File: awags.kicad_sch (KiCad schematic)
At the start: 30 parts

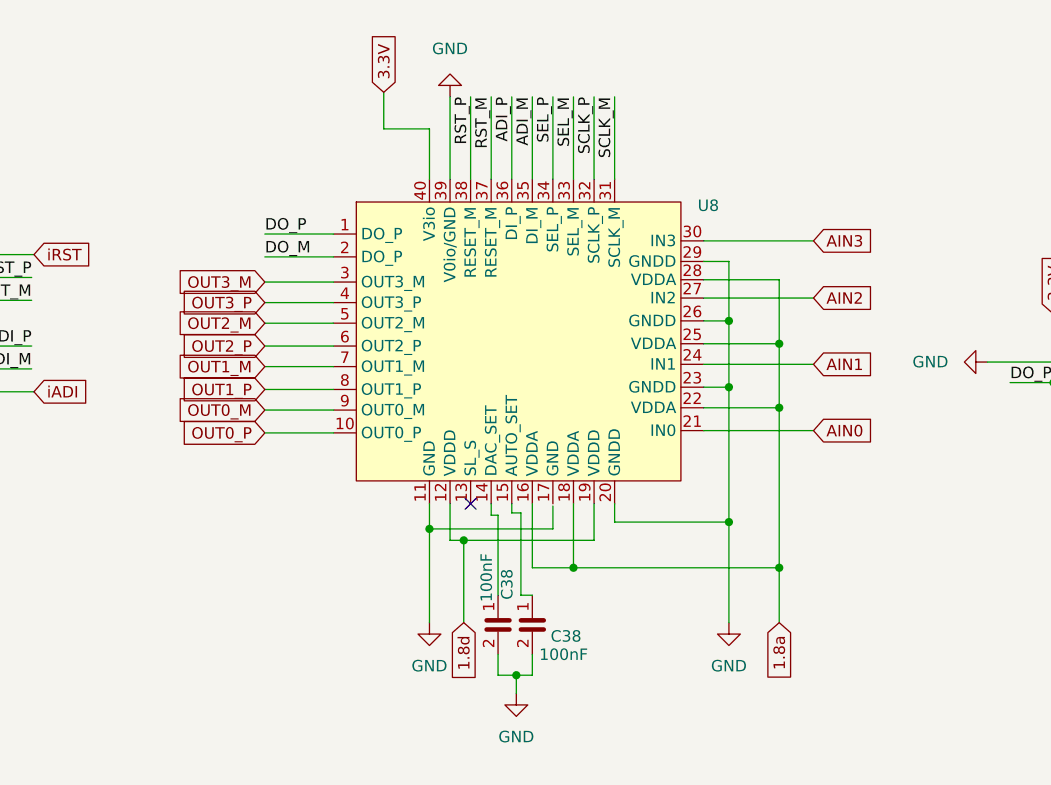
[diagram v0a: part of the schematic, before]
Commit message: Added DAC circuit.
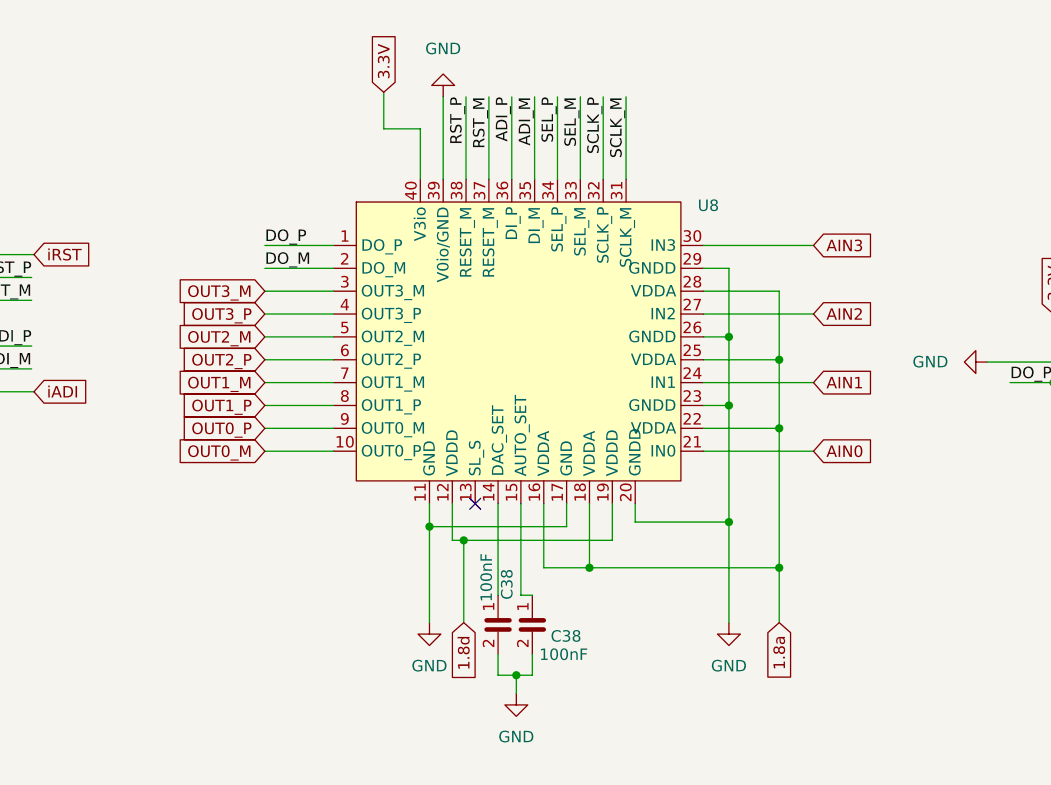
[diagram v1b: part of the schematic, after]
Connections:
- net GND: now also U8.17 (GND)
- net OUT0_M: now also U8.10 (OUT0_P); no longer U8.9 (OUT0_M)
- net OUT0_P: now also U8.9 (OUT0_M); no longer U8.10 (OUT0_P)

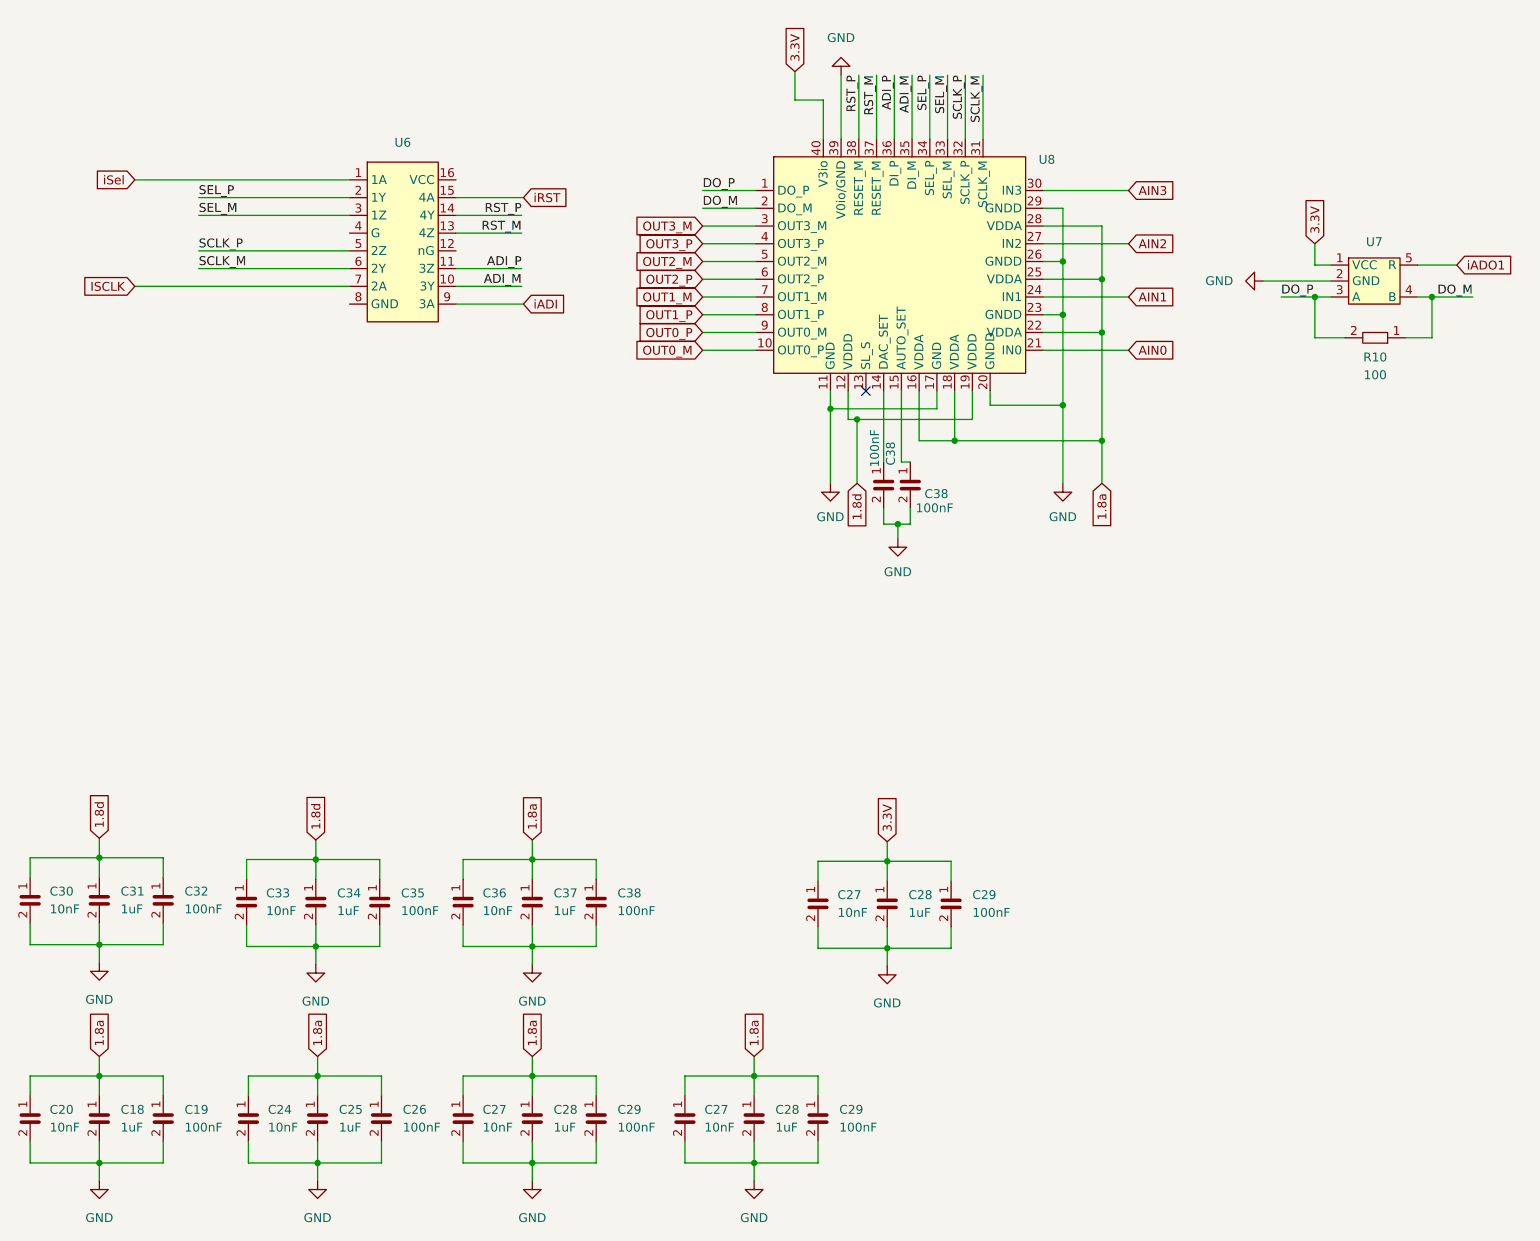
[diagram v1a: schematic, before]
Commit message: Changed global to hierarchichal lables, reorganized main sheet to get pins to connector.
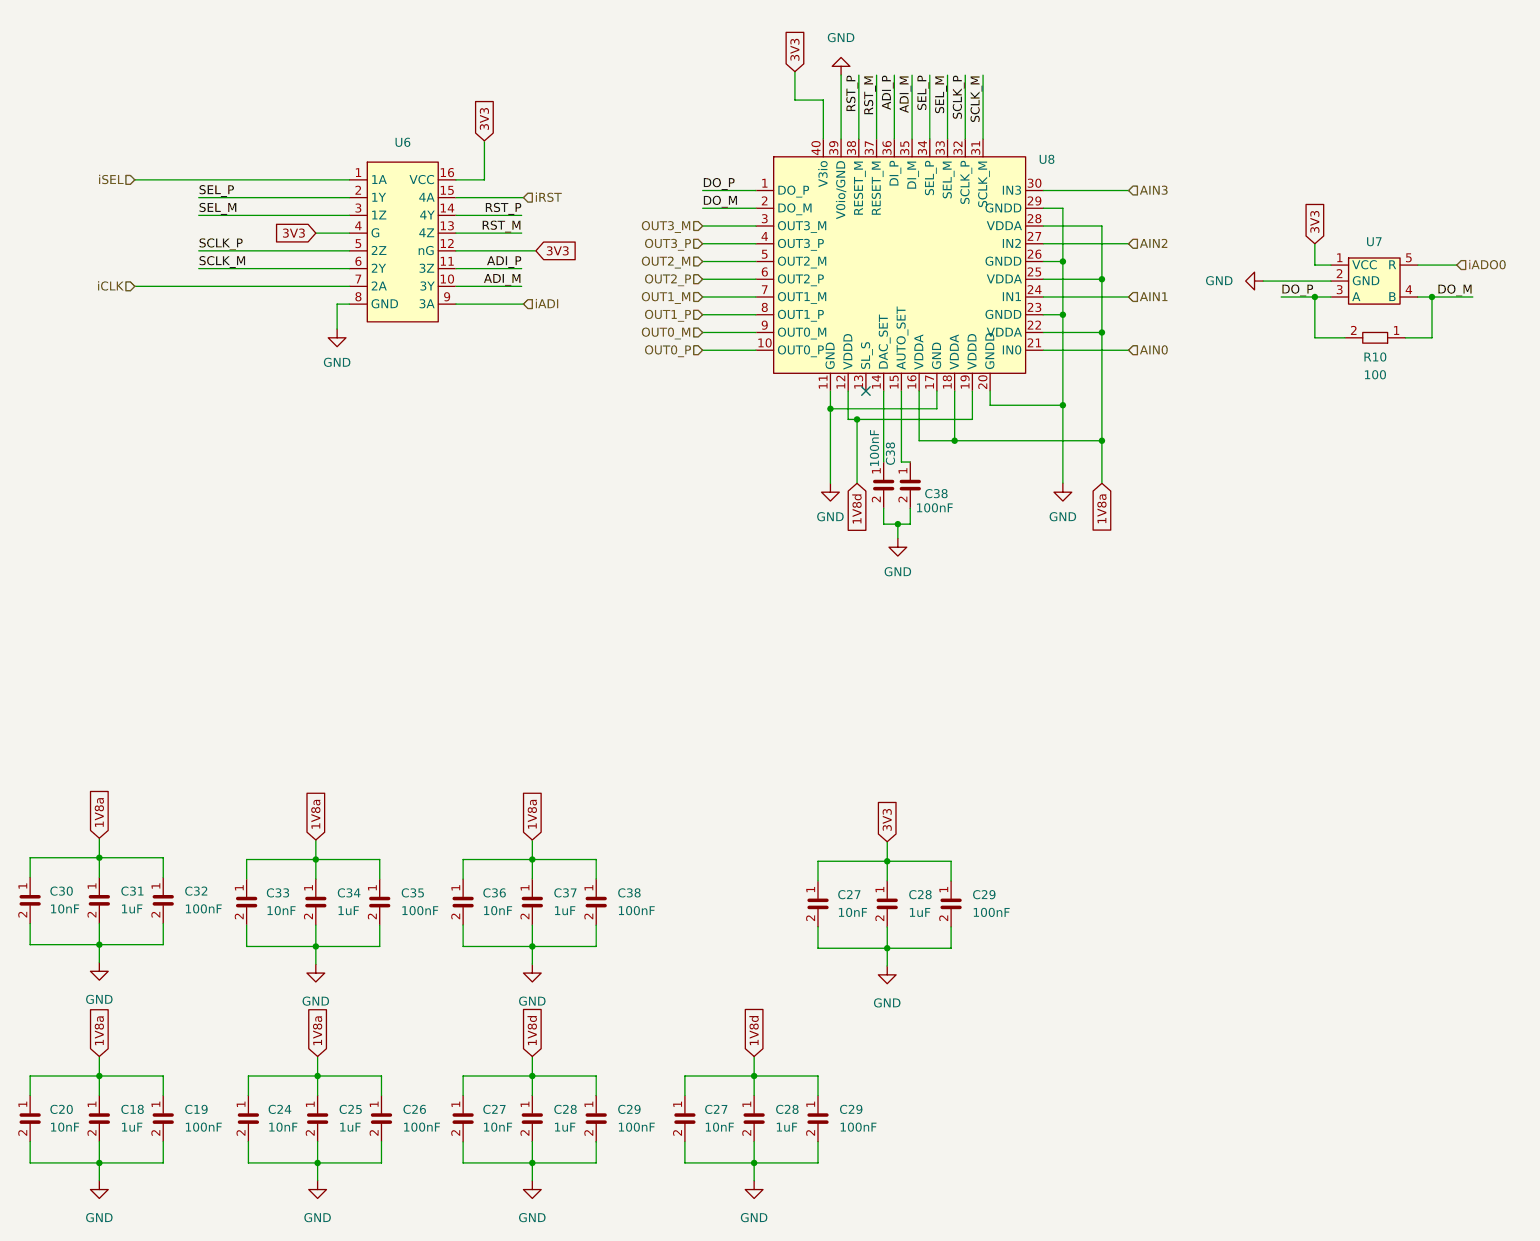
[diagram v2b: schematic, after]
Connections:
- net 3.3V is gone; now on net 3V3: C27.1, C28.1, C29.1, U7.1 (VCC), U8.40 (V3io)
- net GND: now also U6.8 (GND)
- net OUT0_M: now also U8.9 (OUT0_M); no longer U8.10 (OUT0_P)
- net OUT0_P: now also U8.10 (OUT0_P); no longer U8.9 (OUT0_M)
- net 3V3: now reaches U6.12 (nG)
- net 3V3: now also U6.16 (VCC), U6.4 (G)
- net 1.8a renamed 1V8a
- net 1V8a: now also C30.1, C31.1, C32.1, C33.1, C34.1, C35.1; no longer C27.1, C27.1, C28.1, C28.1, C29.1, C29.1
- removed net 1.8d: C30.1, C31.1, C32.1, C33.1, C34.1, C35.1, U8.12 (VDDD), U8.19 (VDDD)
- net ISCLK renamed iCLK
- net iADO1 renamed iADO0
- net iSel renamed iSEL
- new net 1V8d: C27.1, C27.1, C28.1, C28.1, C29.1, C29.1, U8.12 (VDDD), U8.19 (VDDD)

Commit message: Layout erster Entwurf fertig.
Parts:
- removed C18, C28: C0402_1uF_6.3V, Capacitor_SMD:C_0402_1005Metric, symbol Jojos_Lib:C0402_1uF_6.3V
- removed C19, C29: C0402_100nF_50V, Capacitor_SMD:C_0402_1005Metric, symbol Jojos_Lib:C0402_100nF_50V
- removed C20, C27: C0402_10nF_16V, Capacitor_SMD:C_0402_1005Metric, symbol Jojos_Lib:C0402_10nF_16V
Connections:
- net 1V8d is gone; now on net 1V8a: C27.1, C28.1, C29.1, U8.12 (VDDD), U8.19 (VDDD)
- net GND: now also U8.41 (Pad)
